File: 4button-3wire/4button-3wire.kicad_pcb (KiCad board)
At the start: 2 copper layers, 72 x 25.5 mm, 10 parts, among them J1 PCB Audio Jack, SW1 SW_Push_LED_Separate, SW2 SW_Push_LED_Separate, SW3 SW_Push_LED_Separate, SW4 SW_Push_LED_Separate

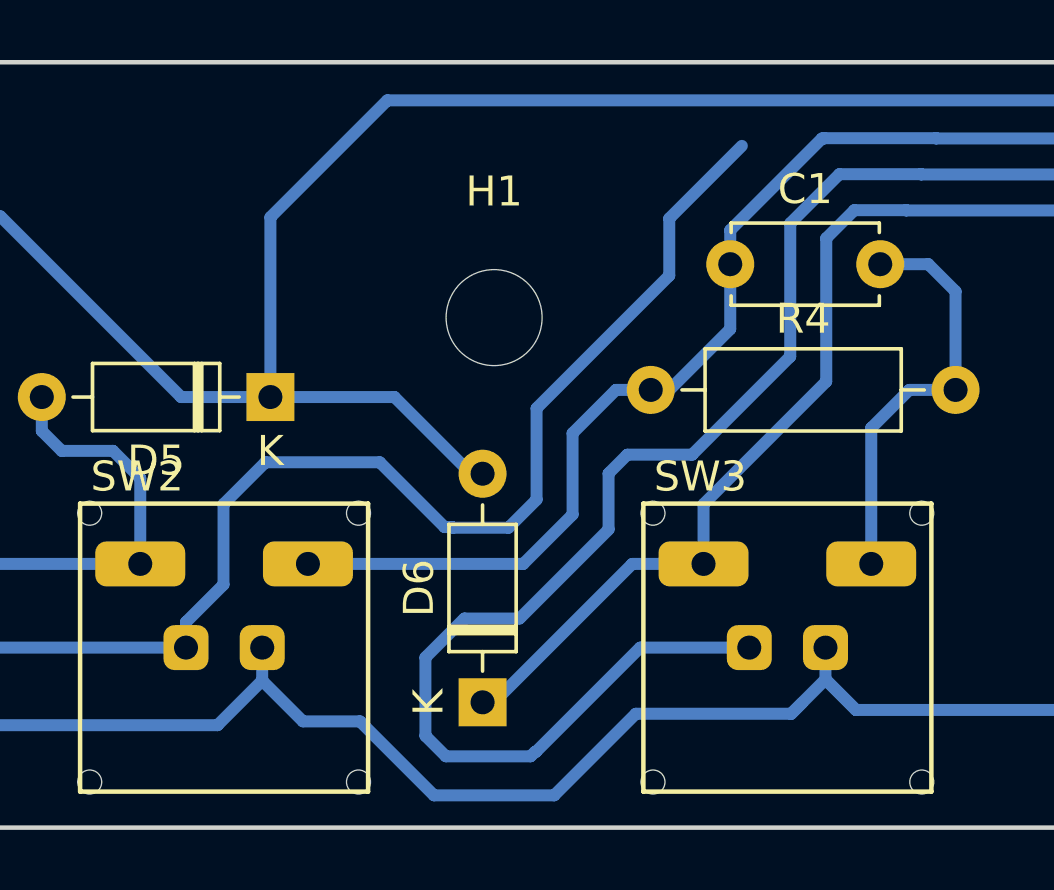
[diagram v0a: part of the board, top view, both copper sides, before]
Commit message: Modified Rules to Add Last Trace
Changed the design rules to allow the last trace to be routed which will require the 1/64" mill bit to be used.

Could use some cleaning up still.
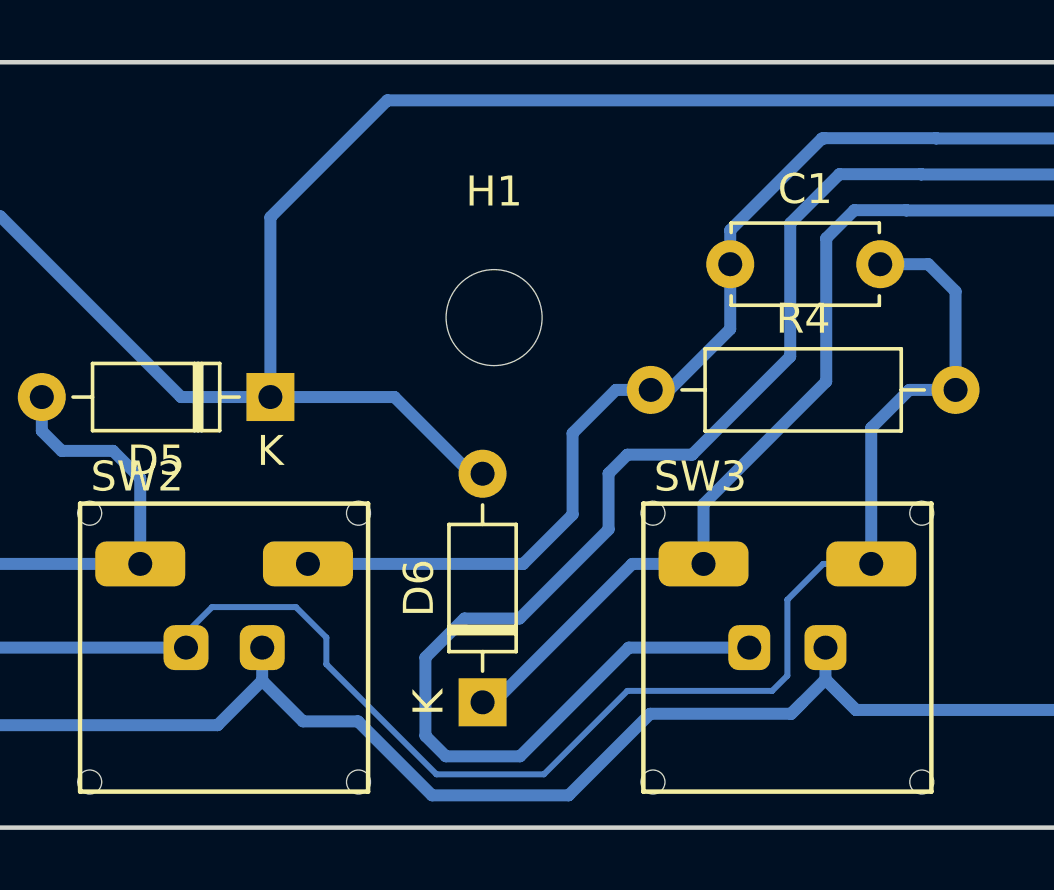
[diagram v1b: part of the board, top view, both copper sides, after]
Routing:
- net Net-(C1-Pad2): track 82.0 -> 80.7 mm
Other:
- net class Small_Mill added: clearance 0.3, trace_width 0.2, via_dia 1, via_drill 0.8

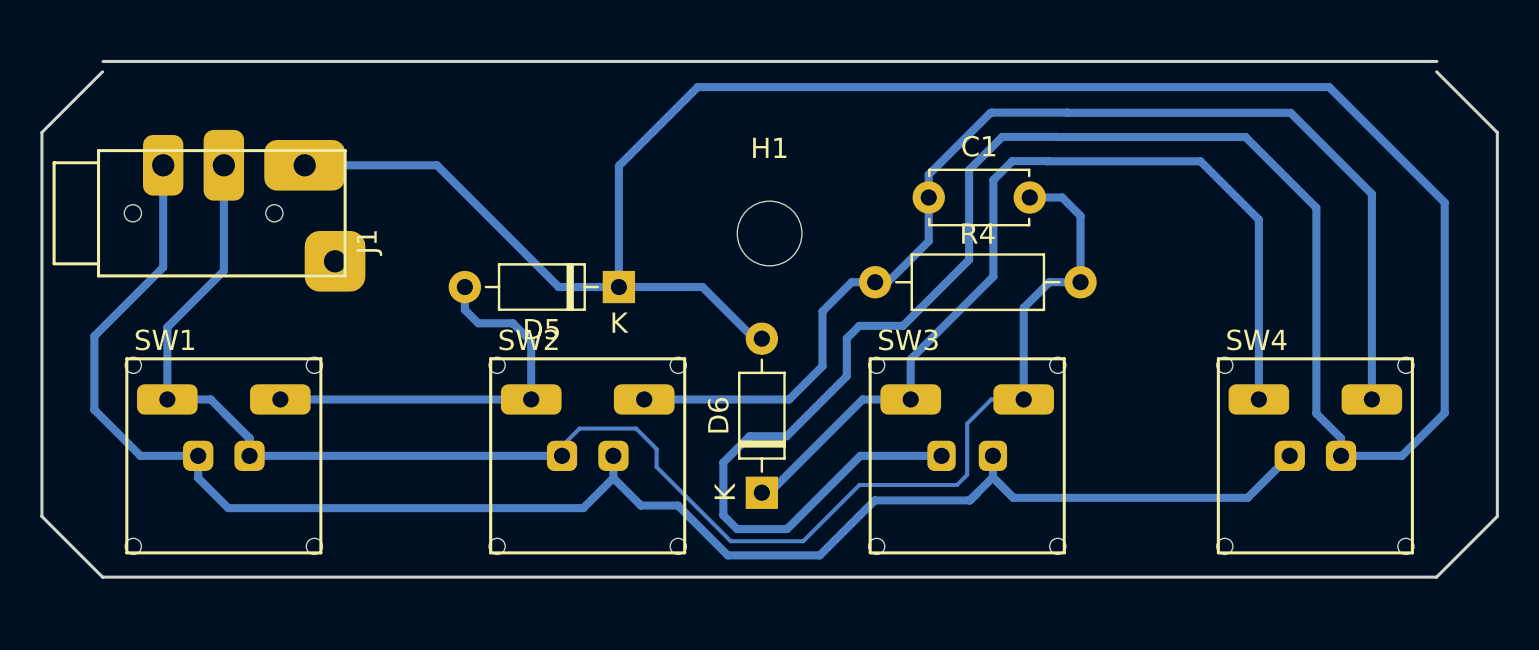
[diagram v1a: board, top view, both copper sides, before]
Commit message: Move Bottom Board Edge Down 1.5mm
A little cleanup to reduce the amount of small spaces.
Closed board outline but not pretty
Moved traces down to open spacing
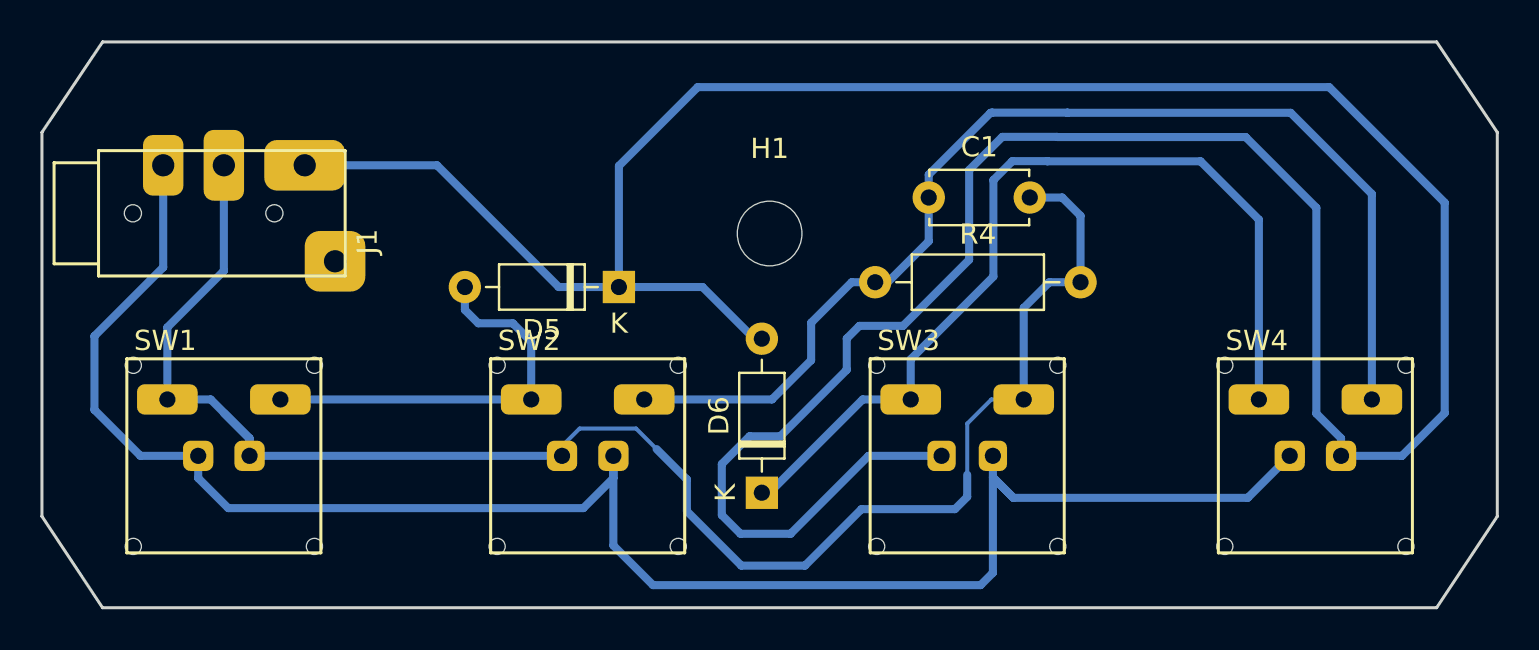
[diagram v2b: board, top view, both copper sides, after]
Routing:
- net Net-(J1-PadS): track 84.4 -> 91.0 mm
- net Net-(C1-Pad2): track 80.7 -> 82.7 mm
- net Net-(C1-Pad1): track 57.2 -> 56.7 mm
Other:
- board size 72 x 25.5 mm -> 72 x 28 mm
